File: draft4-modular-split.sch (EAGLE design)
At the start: 28 parts, among them U2 SPX3819, X1 3v7 lipo, X2 ESP-12, X3 MOD-TP4056

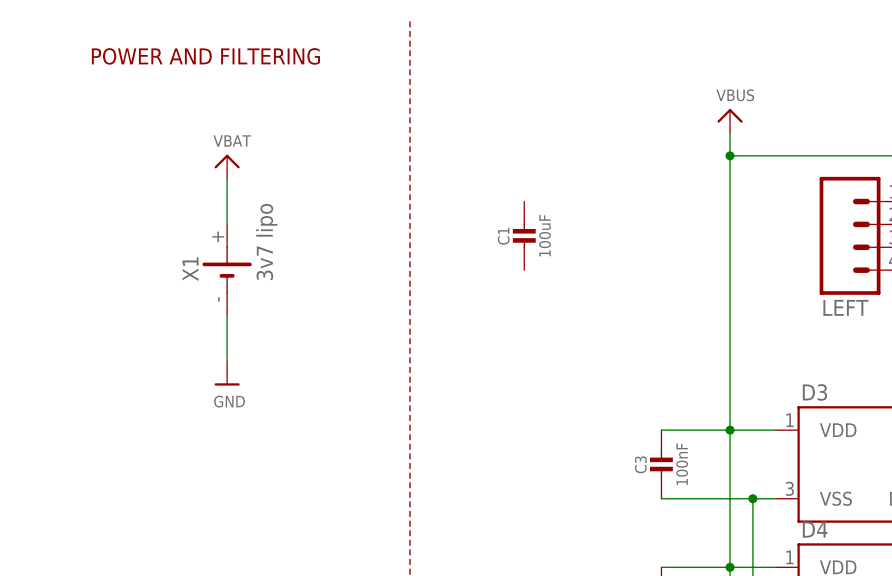
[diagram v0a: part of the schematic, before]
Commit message: updates listed below
* used blossom battery case
* switched to 100uF big fat smds for "bulk" ws2812 support
* fixed values for vbat monitoring divider and added cap to hold it
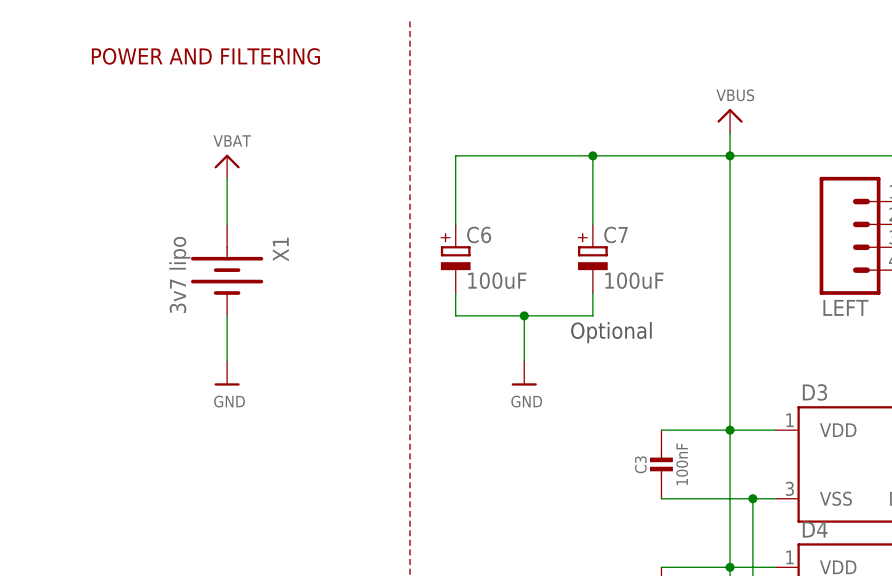
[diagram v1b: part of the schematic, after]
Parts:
- removed C1: 100uF, microbuilder:CAP_CERAMIC_0805
- added C6, C7: 100uF, rcl:CPOL-EUB
- X1: device karls-parts-2016-09:BATTERY -> karls-parts-2016-09:BATTERY18650-BLOSSOM
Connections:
- net GND: now also C6.-, C7.-
- net VBUS: now also C6.+, C7.+
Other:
- note added: "Optional"

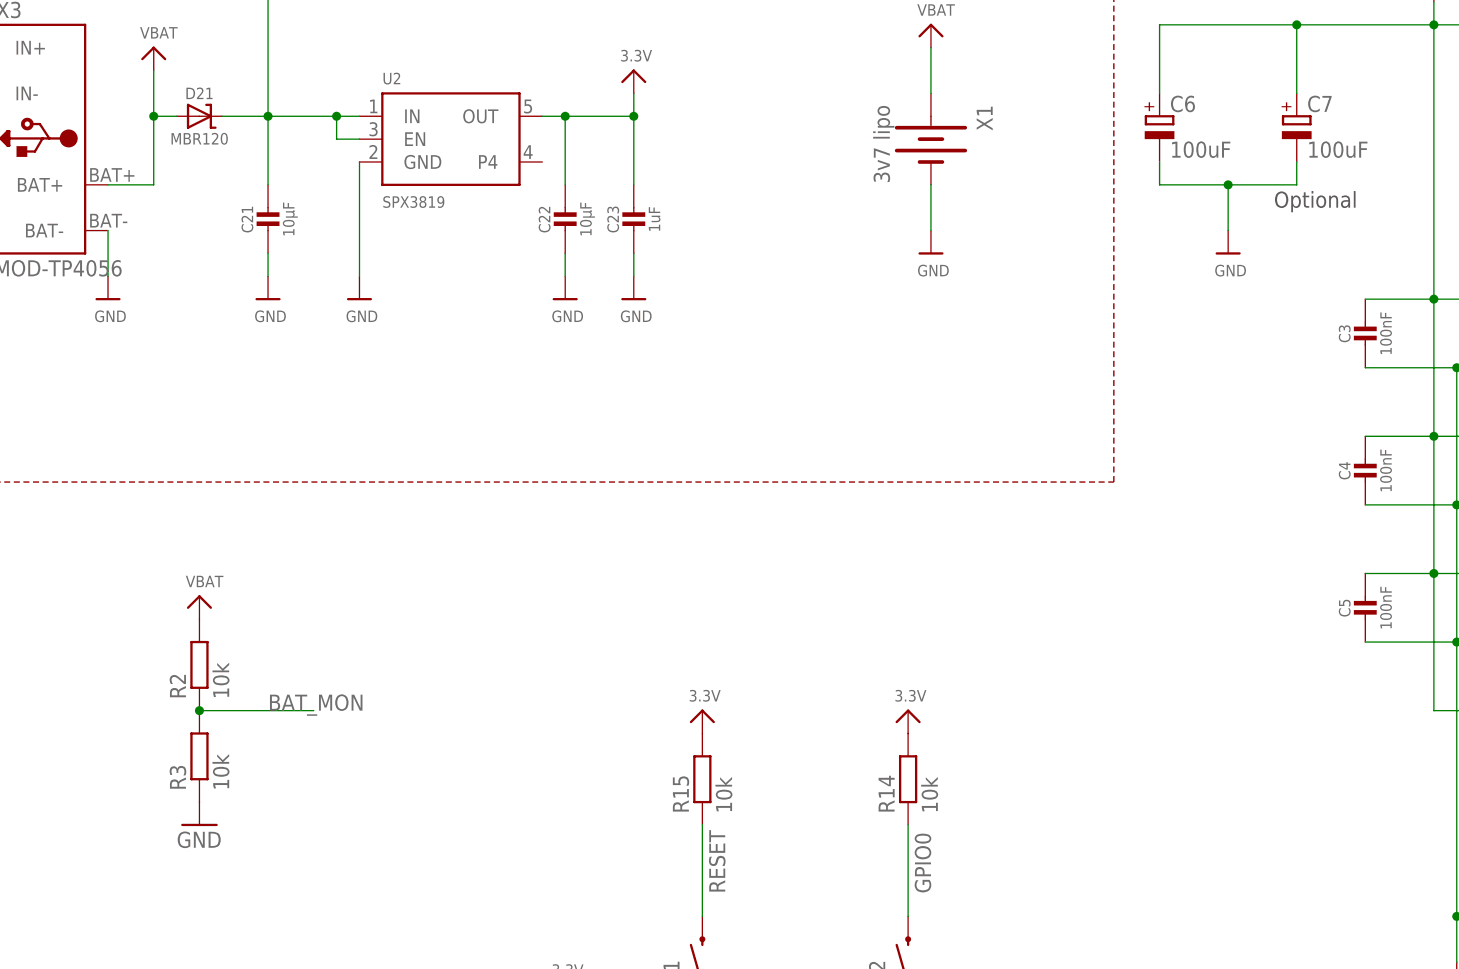
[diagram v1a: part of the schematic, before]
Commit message: updates listed below
* used blossom battery case
* switched to 100uF big fat smds for "bulk" ws2812 support
* fixed values for vbat monitoring divider and added cap to hold it
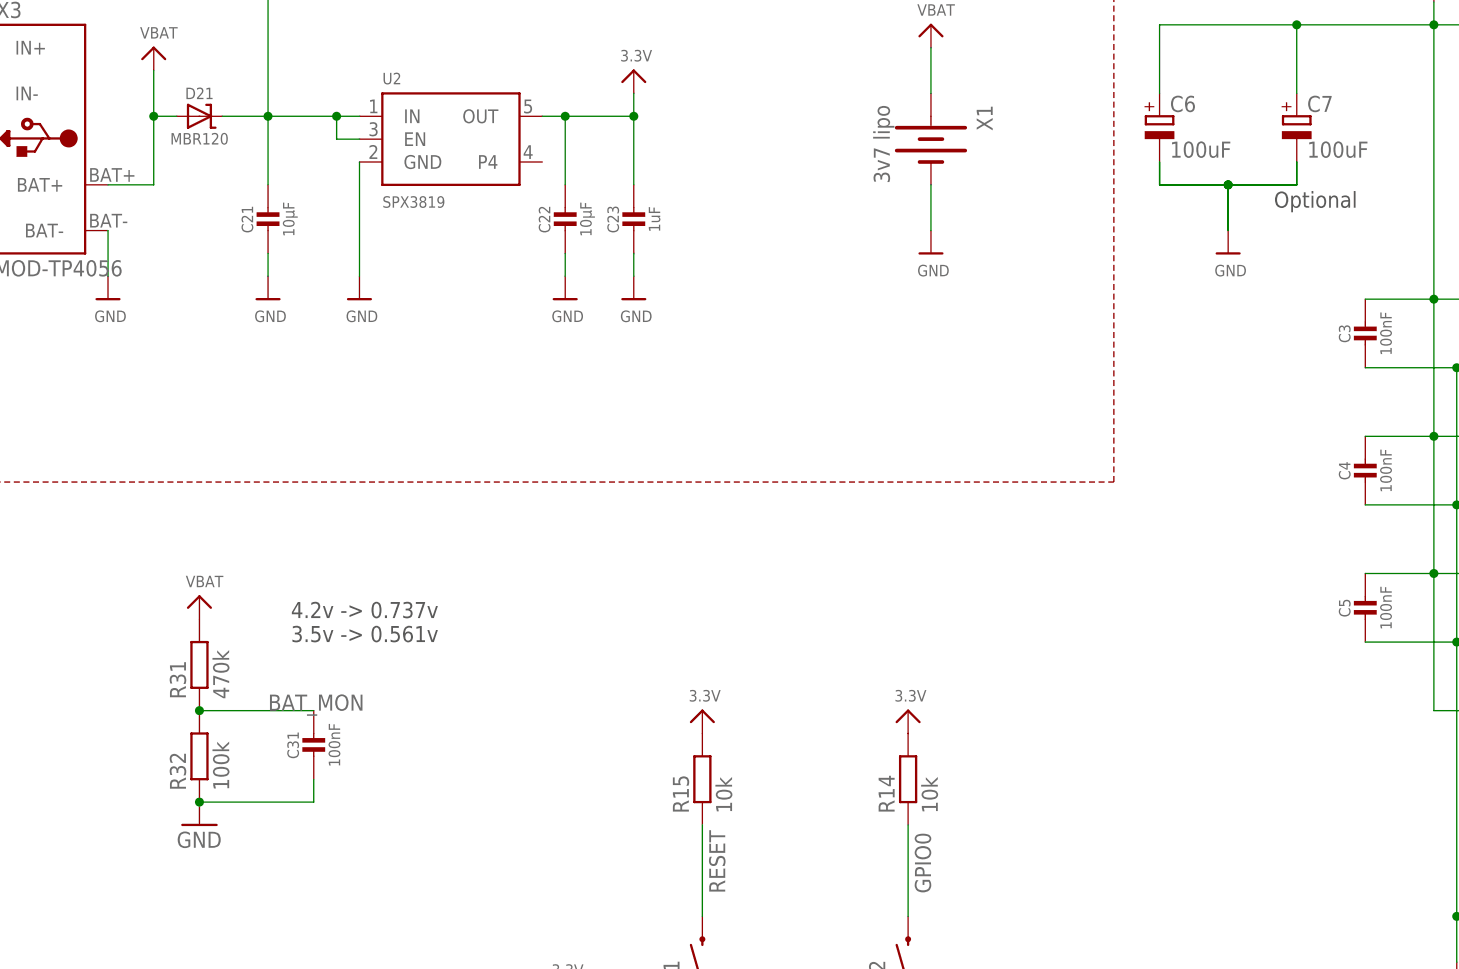
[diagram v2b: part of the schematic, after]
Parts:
- added C31: 100nF, microbuilder:CAP_CERAMIC_0805
- R31: value 10k -> 470k
- R32: value 10k -> 100k
- renumbered R2 to R31, R3 to R32
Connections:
- net BAT_MON: now also C31.1
- net GND: now also C31.2
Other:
- note added: "4.2v -> 0.737v 3.5v -> 0.561v"
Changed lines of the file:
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@@
 <part name="S1" library="SparkFun-Electromechanical" deviceset="SWITCH-MOMENTARY-2" device="PTH" value=""/>
 <part name="S2" library="SparkFun-Electromechanical" deviceset="SWITCH-MOMENTARY-2" device="PTH" value=""/>
-<part name="R2" library="resistor" deviceset="R-EU_" device="R0603" value="10k"/>
-<part name="R3" library="resistor" deviceset="R-EU_" device="R0603" value="10k"/>
+<part name="R31" library="resistor" deviceset="R-EU_" device="R0603" value="470k"/>
+<part name="R32" library="resistor" deviceset="R-EU_" device="R0603" value="100k"/>
 <part name="GND4" library="supply1" deviceset="GND" device=""/>
 <part name="U$14" library="microbuilder" deviceset="VBAT" device=""/>
@@
 <part name="C7" library="rcl" deviceset="CPOL-EU" device="B" value="100uF"/>
 <part name="U$15" library="microbuilder" deviceset="GND" device=""/>
+<part name="C31" library="microbuilder" deviceset="CAP_CERAMIC" device="_0805" value="100nF"/>
 </parts>
 <sheets>
@@
 Lua: GPIO2 only.</text>
 <text x="160.02" y="139.7" size="1.778" layer="97">Optional</text>
+<text x="50.8" y="91.44" size="1.778" layer="97">4.2v -&gt; 0.737v
+3.5v -&gt; 0.561v</text>
 </plain>
 <instances>
@@
 <instance part="S1" gate="G$1" x="96.52" y="55.88" rot="R90"/>
 <instance part="S2" gate="G$1" x="119.38" y="55.88" rot="R90"/>
-<instance part="R2" gate="G$1" x="40.64" y="88.9" rot="R90"/>
-<instance part="R3" gate="G$1" x="40.64" y="78.74" rot="R90"/>
+<instance part="R31" gate="G$1" x="40.64" y="88.9" rot="R90"/>
+<instance part="R32" gate="G$1" x="40.64" y="78.74" rot="R90"/>
 <instance part="GND4" gate="1" x="40.64" y="71.12"/>
 <instance part="U$14" gate="G$1" x="40.64" y="96.52"/>
@@
 <instance part="C7" gate="G$1" x="162.56" y="149.86"/>
 <instance part="U$15" gate="G$1" x="154.94" y="134.62"/>
+<instance part="C31" gate="G$1" x="53.34" y="78.74"/>
 </instances>
 <busses>
@@
 </segment>
 <segment>
-<pinref part="R3" gate="G$1" pin="1"/>
+<pinref part="R32" gate="G$1" pin="1"/>
 <pinref part="GND4" gate="1" pin="GND"/>
+<pinref part="C31" gate="G$1" pin="2"/>
+<wire x1="53.34" y1="76.2" x2="53.34" y2="73.66" width="0.1524" layer="91"/>
+<wire x1="53.34" y1="73.66" x2="40.64" y2="73.66" width="0.1524" layer="91"/>
+<junction x="40.64" y="73.66"/>
+</segment>
+<segment>
+<pinref part="C6" gate="G$1" pin="-"/>
+<pinref part="U$15" gate="G$1" pin="GND"/>
+<wire x1="147.32" y1="144.78" x2="147.32" y2="142.24" width="0.1524" layer="91"/>
+<wire x1="147.32" y1="142.24" x2="154.94" y2="142.24" width="0.1524" layer="91"/>
+<wire x1="154.94" y1="142.24" x2="154.94" y2="137.16" width="0.1524" layer="91"/>
+<pinref part="C7" gate="G$1" pin="-"/>
+<wire x1="162.56" y1="144.78" x2="162.56" y2="142.24" width="0.1524" layer="91"/>
+<wire x1="162.56" y1="142.24" x2="154.94" y2="142.24" width="0.1524" layer="91"/>
+<junction x="154.94" y="142.24"/>
 </segment>
 <segment>
@@
 </segment>
 <segment>
-<pinref part="R2" gate="G$1" pin="2"/>
+<pinref part="R31" gate="G$1" pin="2"/>
 <pinref part="U$14" gate="G$1" pin="VBAT"/>
 </segment>
@@
 <net name="BAT_MON" class="0">
 <segment>
-<pinref part="R2" gate="G$1" pin="1"/>
-<pinref part="R3" gate="G$1" pin="2"/>
+<pinref part="R31" gate="G$1" pin="1"/>
+<pinref part="R32" gate="G$1" pin="2"/>
 <wire x1="40.64" y1="83.82" x2="53.34" y2="83.82" width="0.1524" layer="91"/>
 <junction x="40.64" y="83.82"/>
 <label x="48.26" y="83.82" size="1.778" layer="95"/>
-</segment>
-<segment>
+<pinref part="C31" gate="G$1" pin="1"/>
+</segment>
+<segment>

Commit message: added optional pfet+diode power path instead of diode
fully routed, corrected error with (non)rotated wings.
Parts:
- added D22: MBR120, microbuilder:DIODE-SCHOTTKYSOD-123
- added JP2: JUMPER-PAD-3-2OF3_NC_BY_TRACE_LARGE, SparkFun-Passives:JUMPER-PAD-3-2OF3_NC_BY_TRACE_LARGE
- added Q1: MOSFET-PCHANNEL, SparkFun-DiscreteSemi:MOSFET-PCHANNEL
- added R21: 470k, resistor:R-EU_R0603
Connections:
- new net N$3: D22.C, JP2.3, Q1.D
- new net VSYS: C21.1, C3.1, C4.1, C5.1, C6.+, C7.+, D3.VDD, D4.VDD, D5.VDD, JP2.2, LEFT.1, RIGHT.1, U2.EN, U2.IN
- net GND: now also R21.2
- net VBAT: now also Q1.S
- net VBUS: now also D22.A, JP2.1, Q1.G, R21.1; no longer C21.1, C3.1, C4.1, C5.1, C6.+, C7.+, D3.VDD, D4.VDD, D5.VDD, LEFT.1, RIGHT.1, U2.EN, U2.IN
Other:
- note added: "Optional! GET NEW FOOTPRINTS"
- note added: "Solder to use Schottkey. never cut. no need."
- note added: "With an appropriate pFET, you can reduce the voltage drop (350mV) from the schottkey protection circuitry For load=450mA, RdsON must be less than 770mOhms . AO3401 . DMP3099 . IRLML6401"
- note removed: "Optional"
- moved on the sheet: C21, C22, C23, C31, J1, R14, R15, R31, R32, S1, S2, U2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

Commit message: make all caps consistent footprints
split VSYS into two forks to distribute power better.  even at 1mm wide,
trace resistance is estimted at 300mOhm.  (but that's for the whole
lenght, not longest fork)
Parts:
- C21, C22: value 10µF -> 10uF
- C23: device microbuilder:CAP_CERAMIC0603_NO -> microbuilder:CAP_CERAMIC0805-NOOUTLINE
- C3, C31, C4, C5: device microbuilder:CAP_CERAMIC_0805 -> microbuilder:CAP_CERAMIC0805-NOOUTLINE

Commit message: smash and fix all silk
Add notes on connectors and test points
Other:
- note added: "SUCK TO MY LIBRARY AND FIX"
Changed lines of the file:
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@@
 <text x="50.8" y="119.38" size="1.778" layer="97">Solder to use Schottkey.
 never cut. no need.</text>
+<text x="243.84" y="33.02" size="1.778" layer="97">SUCK TO MY LIBRARY AND FIX</text>
+<text x="223.52" y="15.24" size="1.778" layer="97">SUCK TO MY LIBRARY AND FIX</text>
 </plain>
 <instances>
